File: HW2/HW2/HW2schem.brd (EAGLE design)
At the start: 50 x 50 mm, 21 parts, among them J1 USB_MINI-B_SMT

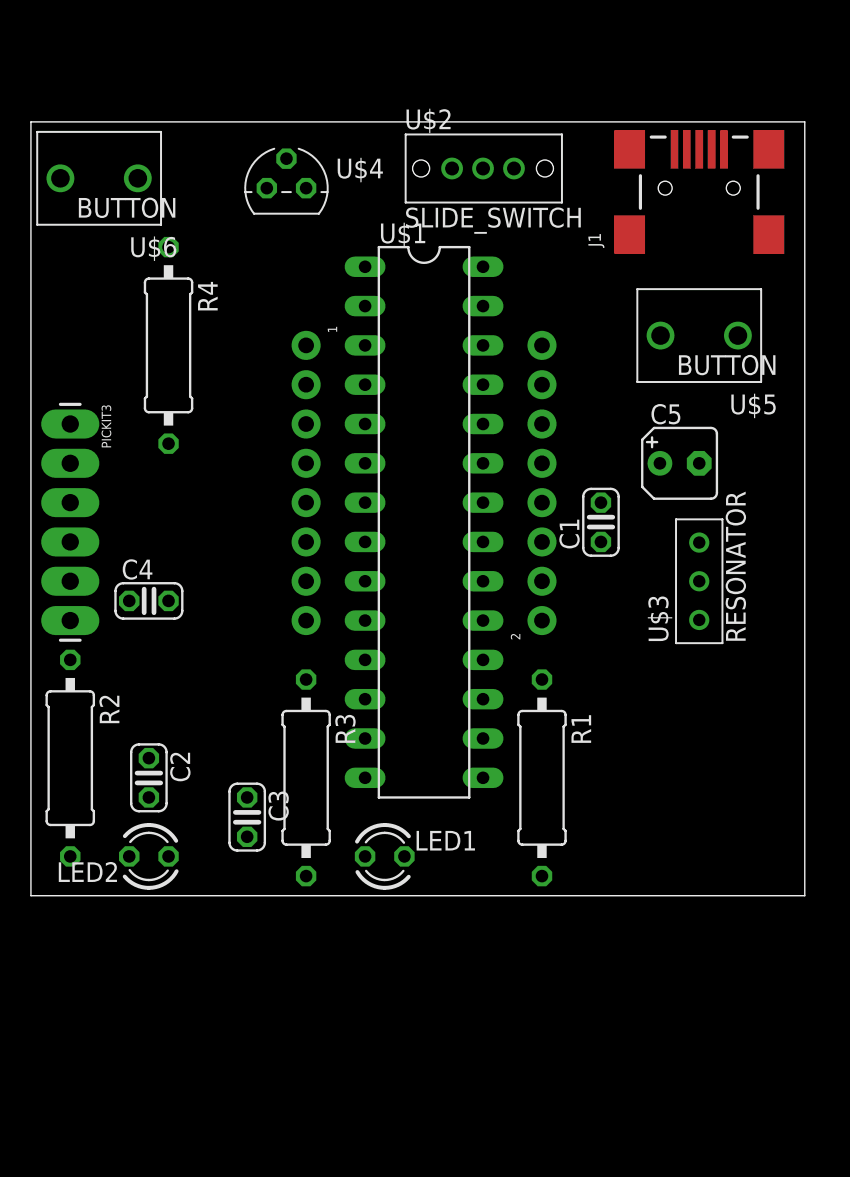
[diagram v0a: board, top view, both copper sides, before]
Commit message: Updated Library and schematic based on released video
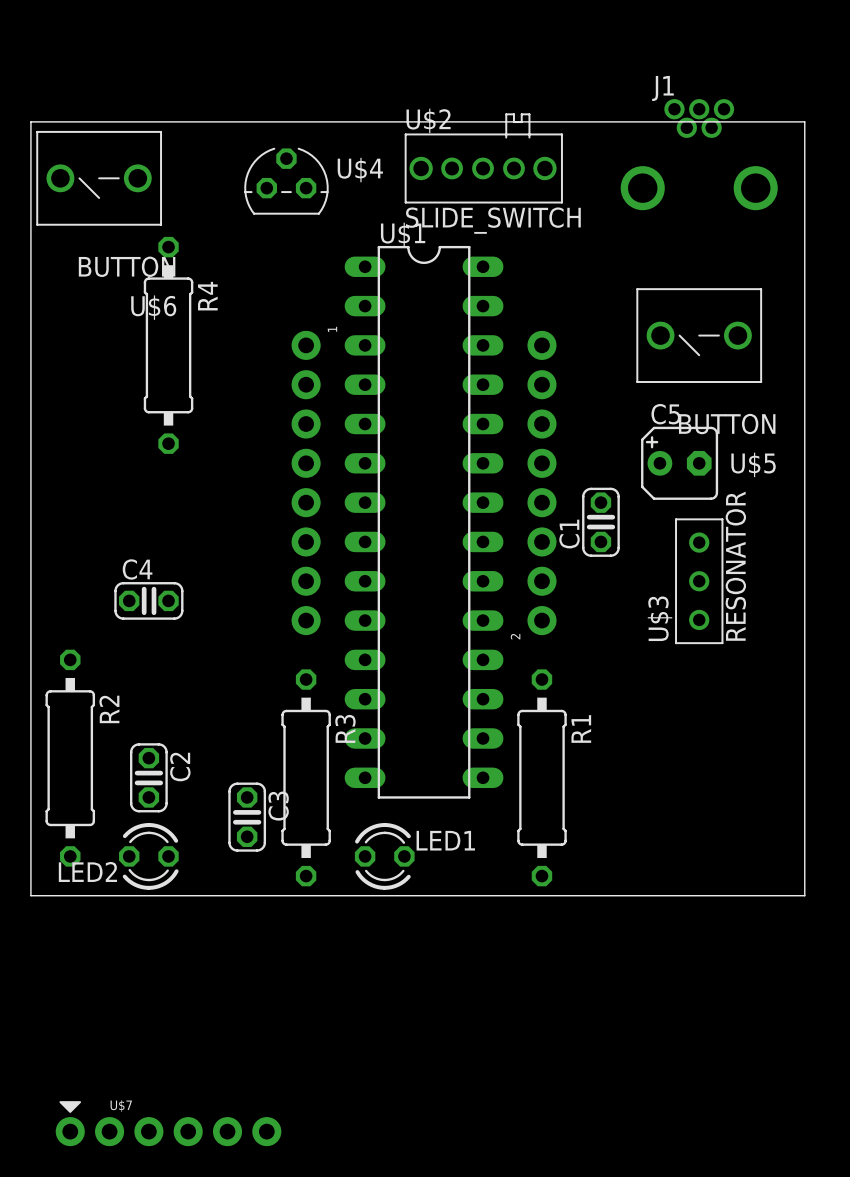
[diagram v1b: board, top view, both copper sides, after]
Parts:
- removed PICKIT3: (no value), HW2Lib:1X06_LONGPADS
- added U$7: PICKIT3, HW2Lib:PICKIT3
- J1: value USB_MINI-B_SMT -> USB_MINI-B; device HW2Lib:USB-MINIB -> HW2Lib:USB-MB-H
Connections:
- removed net VBUS: 2.2, C1.1, U$1.15, U$2.2, U$4.2
- removed net VDD: 1.7, C2.1, C3.2, C4.1, LED2.A, PICKIT3.2, R3.2, R4.2, U$1.13, U$1.23, U$1.28, U$4.3
- new net +3V3: 1.7, C2.1, C3.2, C4.1, LED2.A, R3.2, R4.2, U$1.13, U$1.23, U$1.28, U$4.3, U$7.2
- new net +5V: 2.2, C1.1, U$1.15, U$2.3, U$4.2
- net GND: now also U$7.3; no longer U$2.3
- net N$10: now also U$7.4; no longer PICKIT3.4
- net N$11: now also U$7.5; no longer PICKIT3.5
- net N$2: now also U$7.1; no longer PICKIT3.1
- net N$7: now also U$2.2; no longer U$2.1
- net VSS: no longer PICKIT3.3

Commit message: Rearranged board
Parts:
- R1, R2, R3, R4: device HW2Lib:0309/12 -> HW2Lib:0204/7
- moved U$7 63.5 mm to (1.27, 48.3), turned to 270 degrees
- moved R3 38.3 mm to (9.20, 44.9), turned to 90 degrees
- moved U$5 29.7 mm to (15.2, 46.4), turned to 0 degrees
- moved U$3 28.8 mm to (14.6, 16.5)
- moved C5 27.7 mm to (15.9, 37.5), turned to 90 degrees
- moved R1 27.6 mm to (5.54, 4.74), turned to 0 degrees
- moved C1 21.3 mm to (16.5, 30.5)
- moved U$6 19.7 mm to (24.1, 46.4)
- moved U$4 18.5 mm to (34.3, 40.6), turned to 180 degrees
- moved 1 16.6 mm to (1.27, 34.3)
- moved 2 16.6 mm to (49.5, 16.5)
- moved R4 10.1 mm to (6.07, 45.3)
- moved R2 7.25 mm to (5.54, 2.29), turned to 0 degrees
- moved C2 5.24 mm to (6.35, 12.7)
- moved C3 5.12 mm to (18.4, 7.62)
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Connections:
- removed net VSS: C3.1, U$1.8
- net GND: now also C3.1, U$1.8

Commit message: Finished tentative board, added sick logo
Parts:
- moved C5 27.9 mm to (34.3, 16.5), turned to 0 degrees
- moved C1 18.2 mm to (34.3, 34.3), turned to 270 degrees
- moved C4 8.91 mm to (8.26, 8.89)
- moved C2 7.41 mm to (12.7, 8.89)
- moved C3 1.80 mm to (17.1, 8.89)
- moved 2 0.76 mm to (48.8, 16.5)
- moved R4 0.36 mm to (6.00, 44.9), turned to 90 degrees
- turned LED1 to 180 degrees
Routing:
- net +3V3: track 0.00 -> 117.8 mm, vias 0 -> 5
- net +5V: track 0.00 -> 65.5 mm, vias 0 -> 1
- net B4: track 0.00 -> 61.5 mm
- net ID: track 0.00 -> 60.6 mm, vias 0 -> 2
- net D+: track 0.00 -> 34.9 mm
- net N$2: track 0.00 -> 33.5 mm, vias 0 -> 1
- net A4: track 0.00 -> 33.0 mm
- net D-: track 0.00 -> 32.8 mm, vias 0 -> 1
- net N$10: track 0.00 -> 28.0 mm, vias 0 -> 1
- net N$11: track 0.00 -> 26.5 mm, vias 0 -> 1
- net B9: track 0.00 -> 25.9 mm
- net B8: track 0.00 -> 25.9 mm
- net B7: track 0.00 -> 25.9 mm
- net B3: track 0.00 -> 22.4 mm
- net B2: track 0.00 -> 22.4 mm
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- added copper zone on layer 16, net GND
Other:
- board text added: "3V3"
- board text added: "5V"
- board text added: "A0"
- board text added: "A1"
- board text added: "A4"
- board text added: "B13"
- board text added: "B14"
- board text added: "B15"
- board text added: "B2"
- board text added: "B3"
- board text added: "B4"
- board text added: "B7"
- board text added: "B8"
- board text added: "B9"
- board text added: "CLR"
- board text added: "GND"
- board text added: "USER"
- board text added: "soundcloud.com/hyraxe"
